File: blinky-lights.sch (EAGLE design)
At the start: 16 parts, among them U1 555, U2 A2678EAT

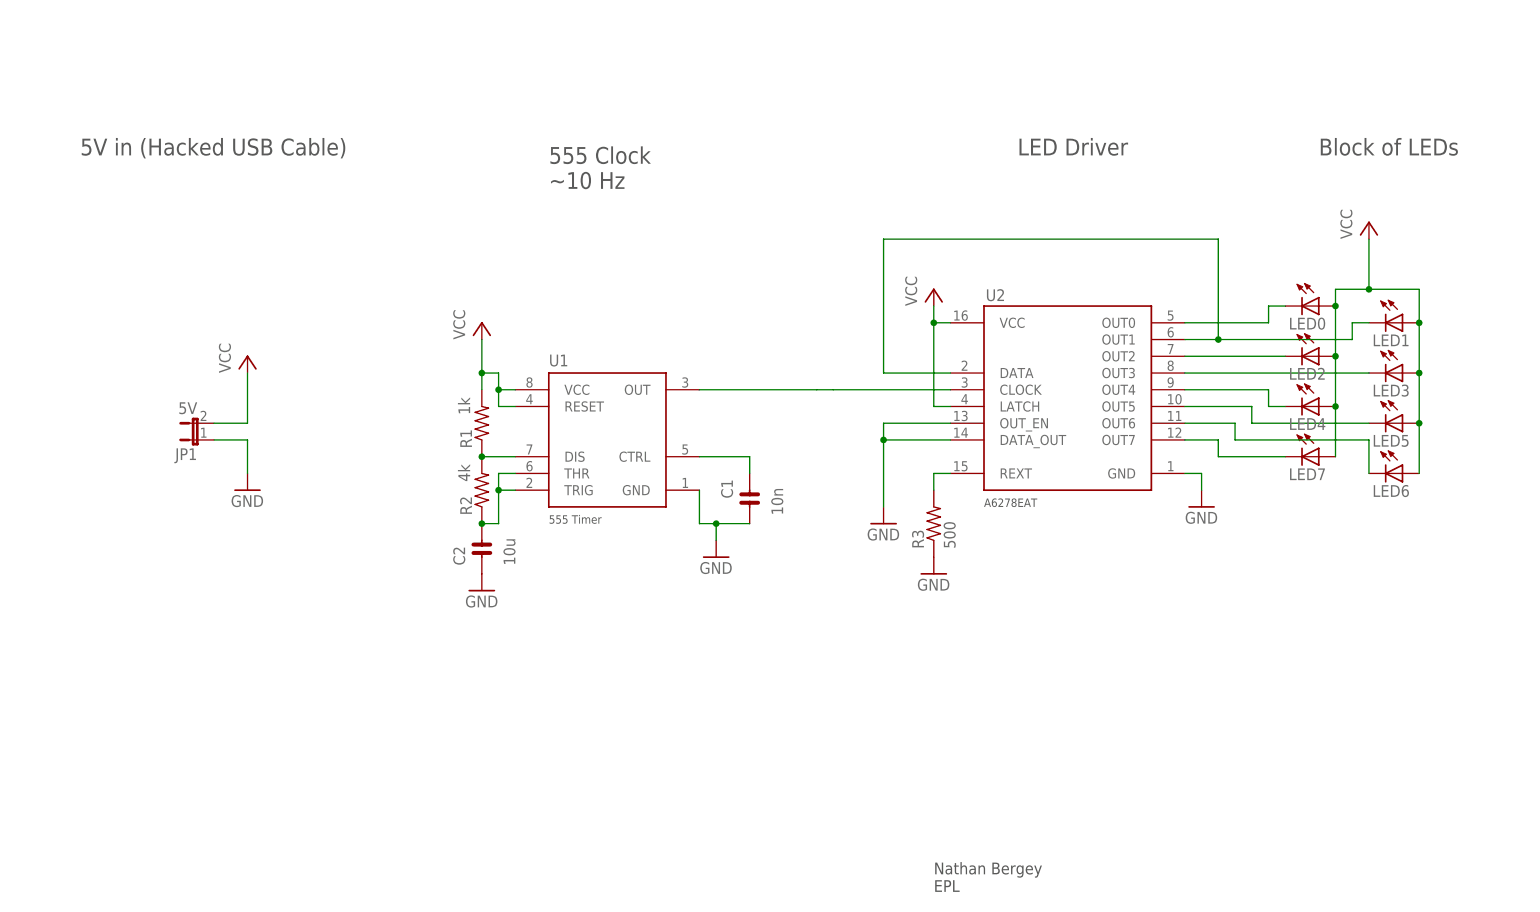
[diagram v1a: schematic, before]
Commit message: Feedback with a NPN transistor and pulldown resistor on DATA line. Also added decoupling capacitor at power in
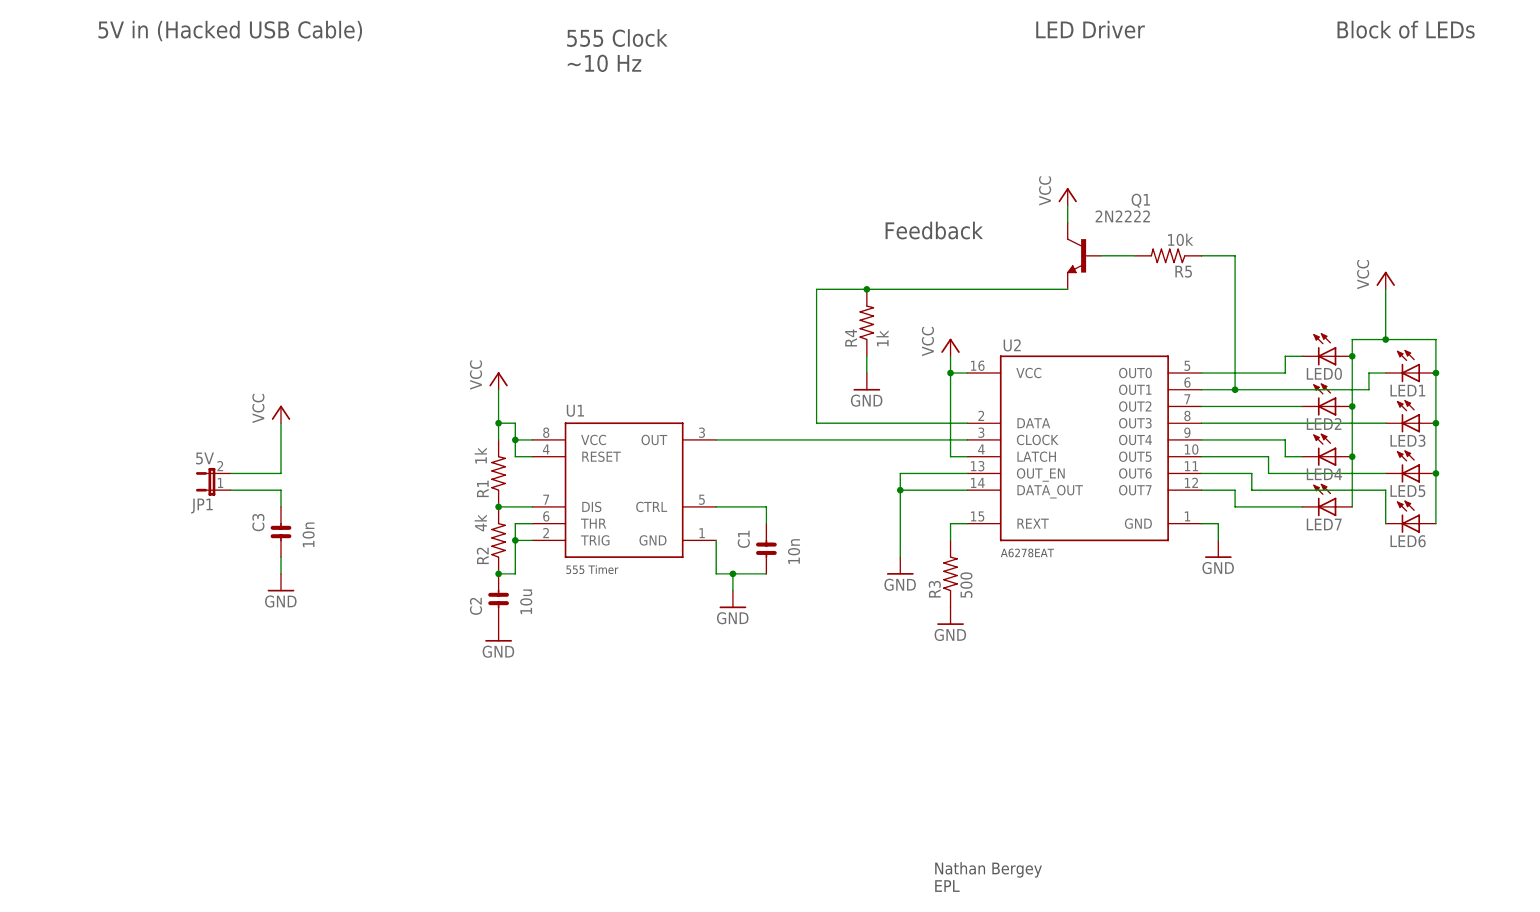
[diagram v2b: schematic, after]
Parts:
- added C3: 10n, blinky-lights:CAP
- added Q1: 2N2222, transistor-neu-to92:2N2222
- added R4: 1k, rcl:R-US_VTA55
- added R5: 10k, rcl:R-US_VTA55
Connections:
- new net FEEDBACK: LED1.C, R5.1, U2.OUT1
- new net N$12: Q1.B, R5.2
- new net N$13: C3.A, JP1.1
- net DATA: now also Q1.E, R4.2; no longer LED1.C, U2.OUT1
- net GND: now also C3.C, R4.1; no longer JP1.1
- net VCC: now also Q1.C
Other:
- note added: "Feedback"
- moved on the sheet: C1, C2, JP1, LED0, LED1, LED2, LED3, LED4, LED5, LED6, LED7, R1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

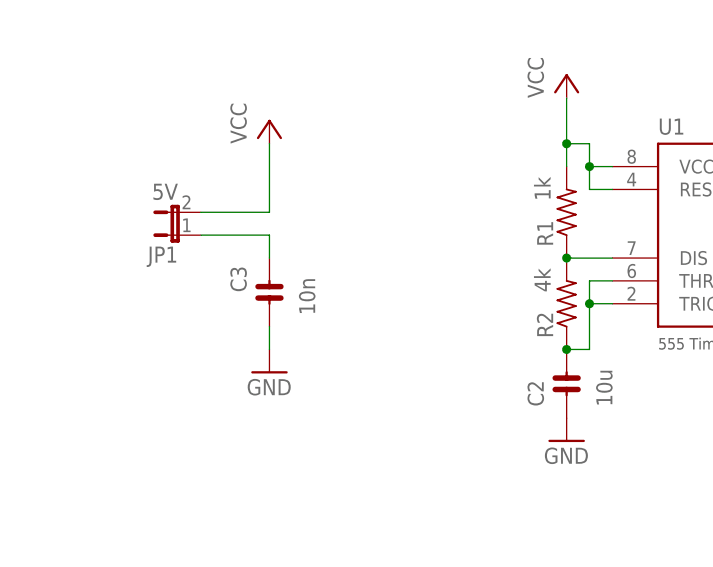
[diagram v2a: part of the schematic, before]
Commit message: Capacitor Value
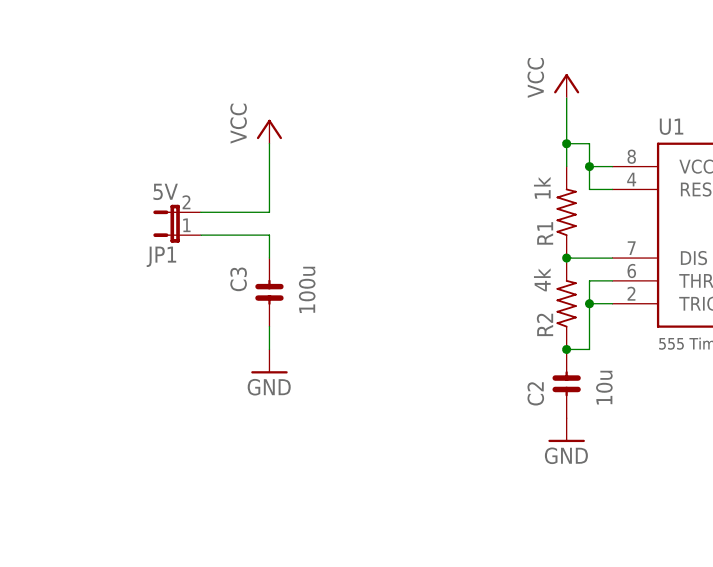
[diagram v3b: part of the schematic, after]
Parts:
- C3: value 10n -> 100u
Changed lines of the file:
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@@
 <part name="P+5" library="supply1" deviceset="VCC" device=""/>
 <part name="R5" library="rcl" deviceset="R-US_" device="VTA55" value="10k"/>
-<part name="C3" library="blinky-lights" deviceset="CAP" device="" value="10n"/>
+<part name="C3" library="blinky-lights" deviceset="CAP" device="" value="100u"/>
 </parts>
 <sheets>

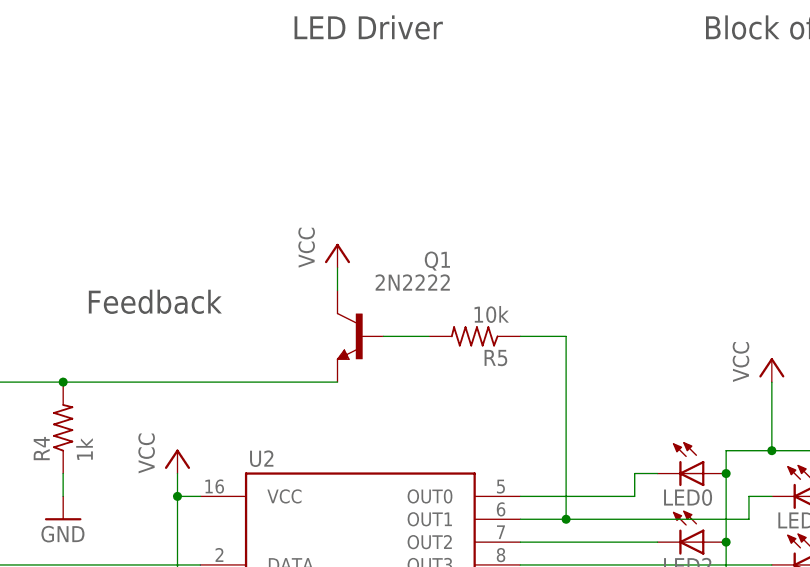
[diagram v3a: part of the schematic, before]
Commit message: first pass board layout with not routing
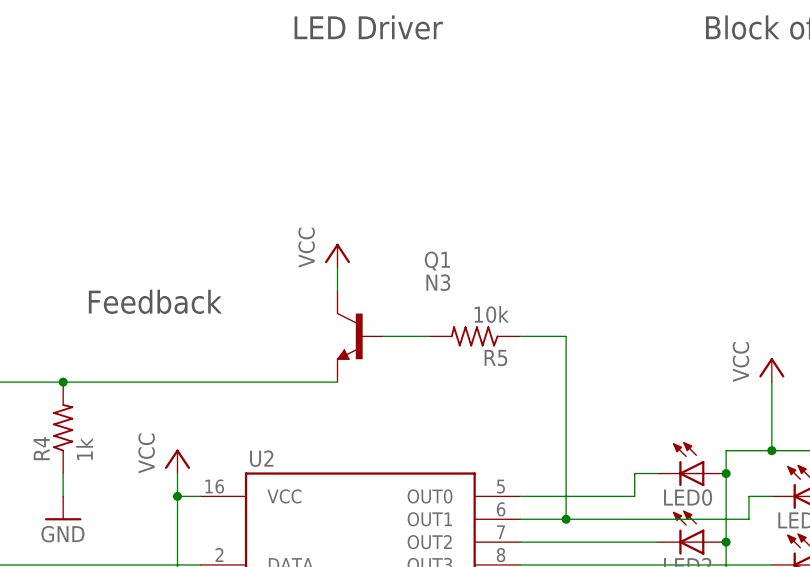
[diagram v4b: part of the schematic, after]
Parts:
- Q1: value 2N2222 -> N3; device transistor-neu-to92:2N2222 -> blinky-lights:N3
- R1, R2, R3, R4, R5: device rcl:R-US_VTA55 -> rcl:R-US_VMTB60
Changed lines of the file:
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@@
 <part name="GND1" library="supply1" deviceset="GND" device=""/>
 <part name="GND3" library="supply1" deviceset="GND" device=""/>
-<part name="R3" library="rcl" deviceset="R-US_" device="VTA55" value="500"/>
-<part name="R1" library="rcl" deviceset="R-US_" device="VTA55" value="1k"/>
-<part name="R2" library="rcl" deviceset="R-US_" device="VTA55" value="4k"/>
+<part name="R3" library="rcl" deviceset="R-US_" device="VMTB60" value="500"/>
+<part name="R1" library="rcl" deviceset="R-US_" device="VMTB60" value="1k"/>
+<part name="R2" library="rcl" deviceset="R-US_" device="VMTB60" value="4k"/>
 <part name="GND4" library="supply1" deviceset="GND" device=""/>
 <part name="GND5" library="supply1" deviceset="GND" device=""/>
@@
 <part name="GND6" library="supply1" deviceset="GND" device=""/>
 <part name="GND2" library="supply1" deviceset="GND" device=""/>
-<part name="Q1" library="transistor-neu-to92" deviceset="2N2222" device=""/>
-<part name="R4" library="rcl" deviceset="R-US_" device="VTA55" value="1k"/>
+<part name="Q1" library="blinky-lights" deviceset="N3*" device=""/>
+<part name="R4" library="rcl" deviceset="R-US_" device="VMTB60" value="1k"/>
 <part name="GND7" library="supply1" deviceset="GND" device=""/>
 <part name="P+5" library="supply1" deviceset="VCC" device=""/>
-<part name="R5" library="rcl" deviceset="R-US_" device="VTA55" value="10k"/>
+<part name="R5" library="rcl" deviceset="R-US_" device="VMTB60" value="10k"/>
 <part name="C3" library="blinky-lights" deviceset="CAP" device="" value="100u"/>
 </parts>
